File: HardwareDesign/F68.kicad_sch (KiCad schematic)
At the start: 2 parts, among them J001 Conn_02x40_Odd_Even

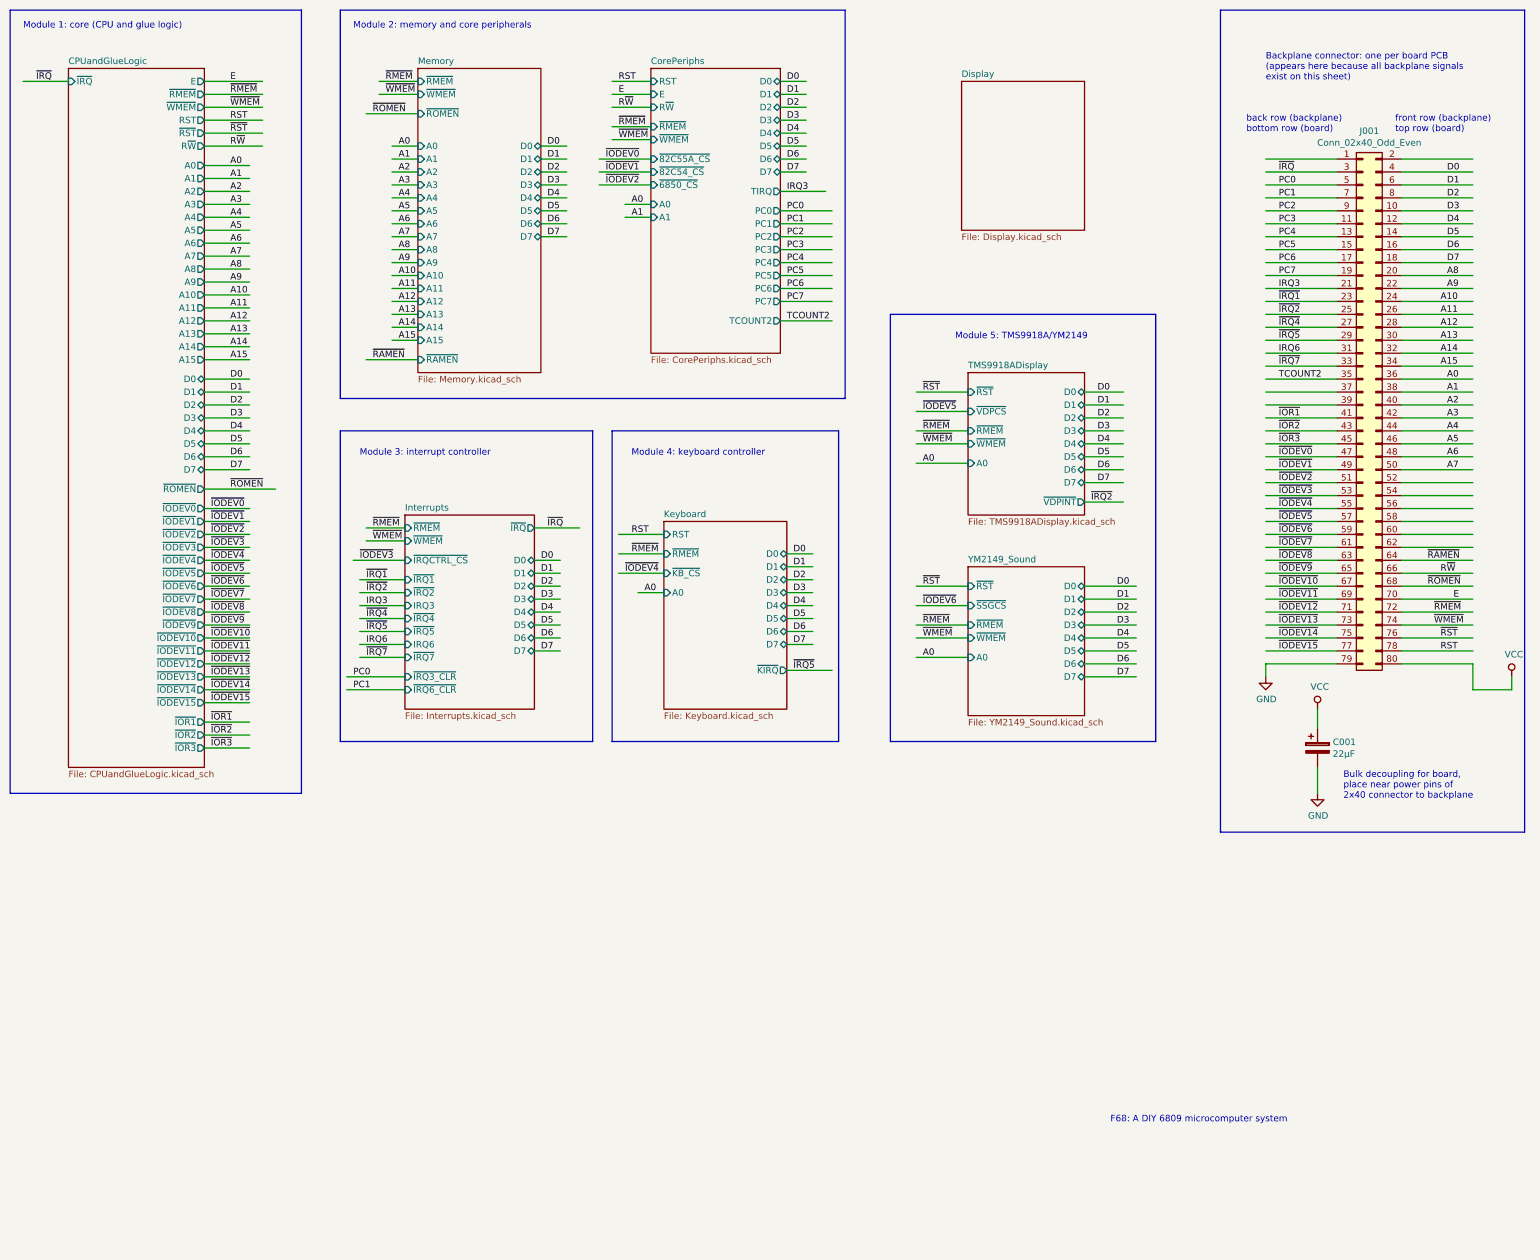
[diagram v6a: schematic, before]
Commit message: initial schematic for FPGA display controller
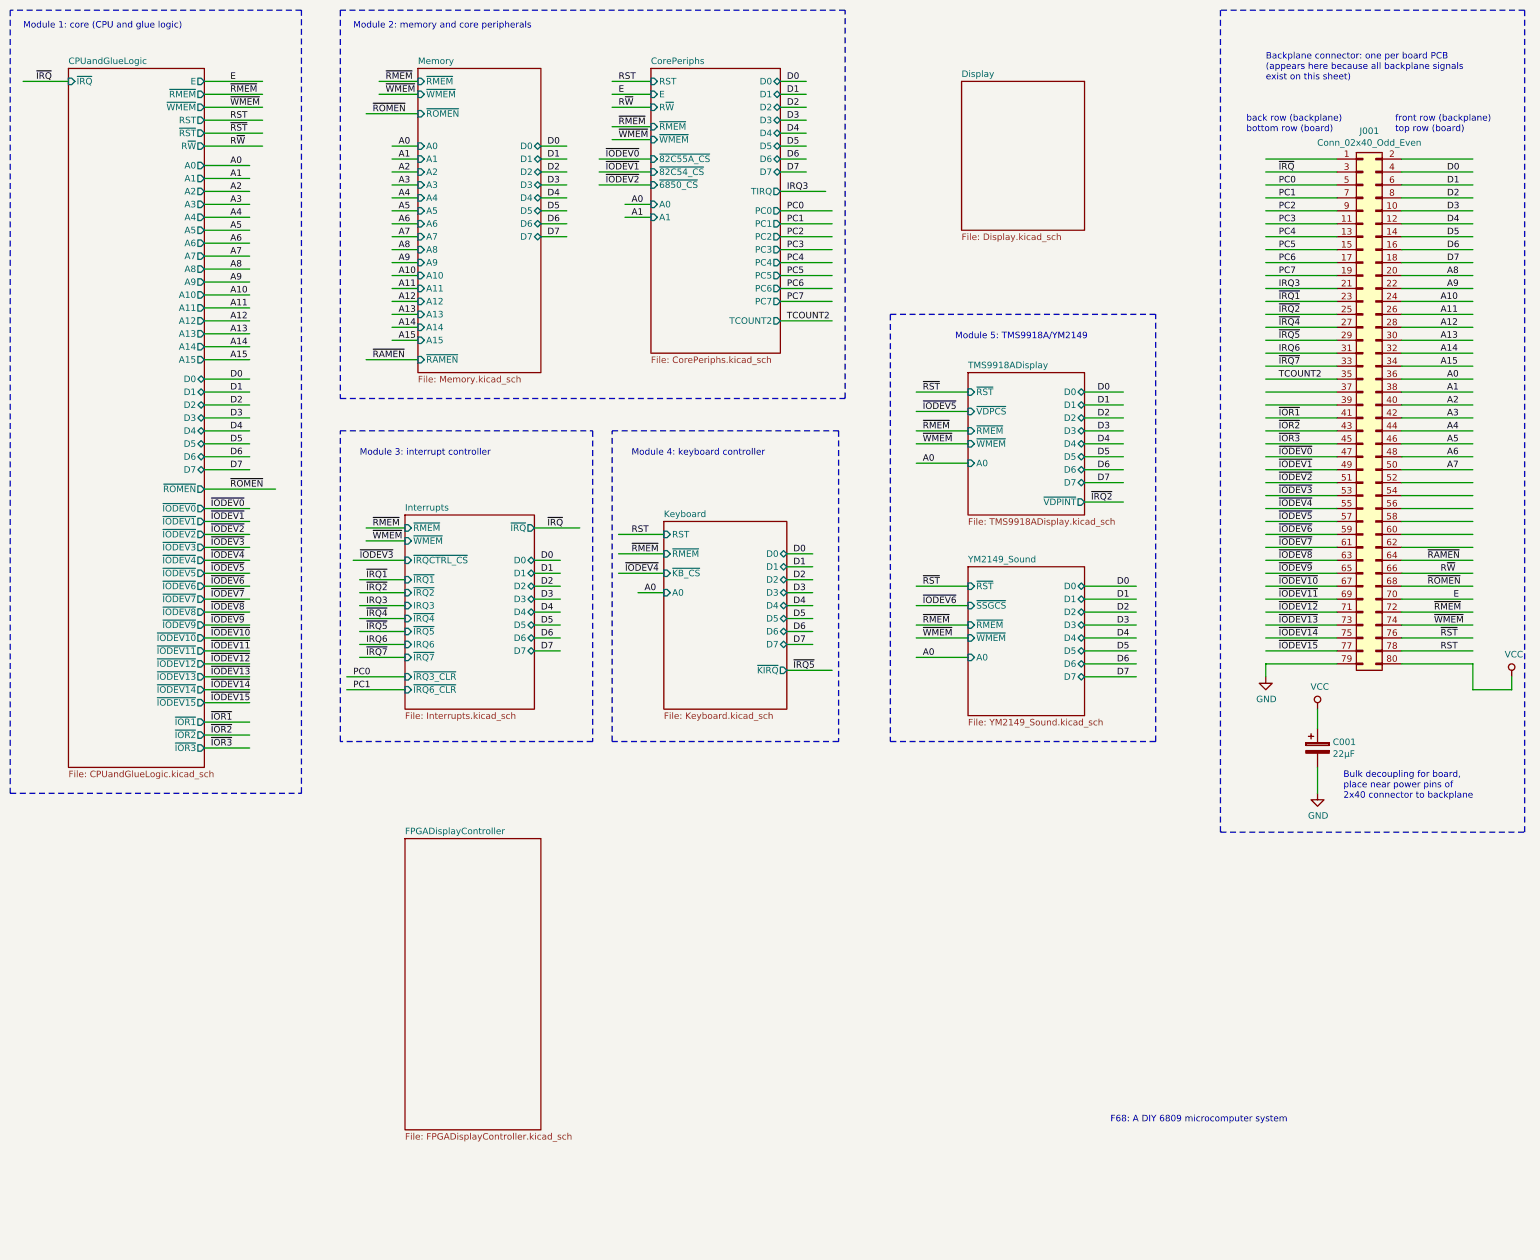
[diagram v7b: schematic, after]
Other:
- added sheet FPGADisplayController (FPGADisplayController.kicad_sch)

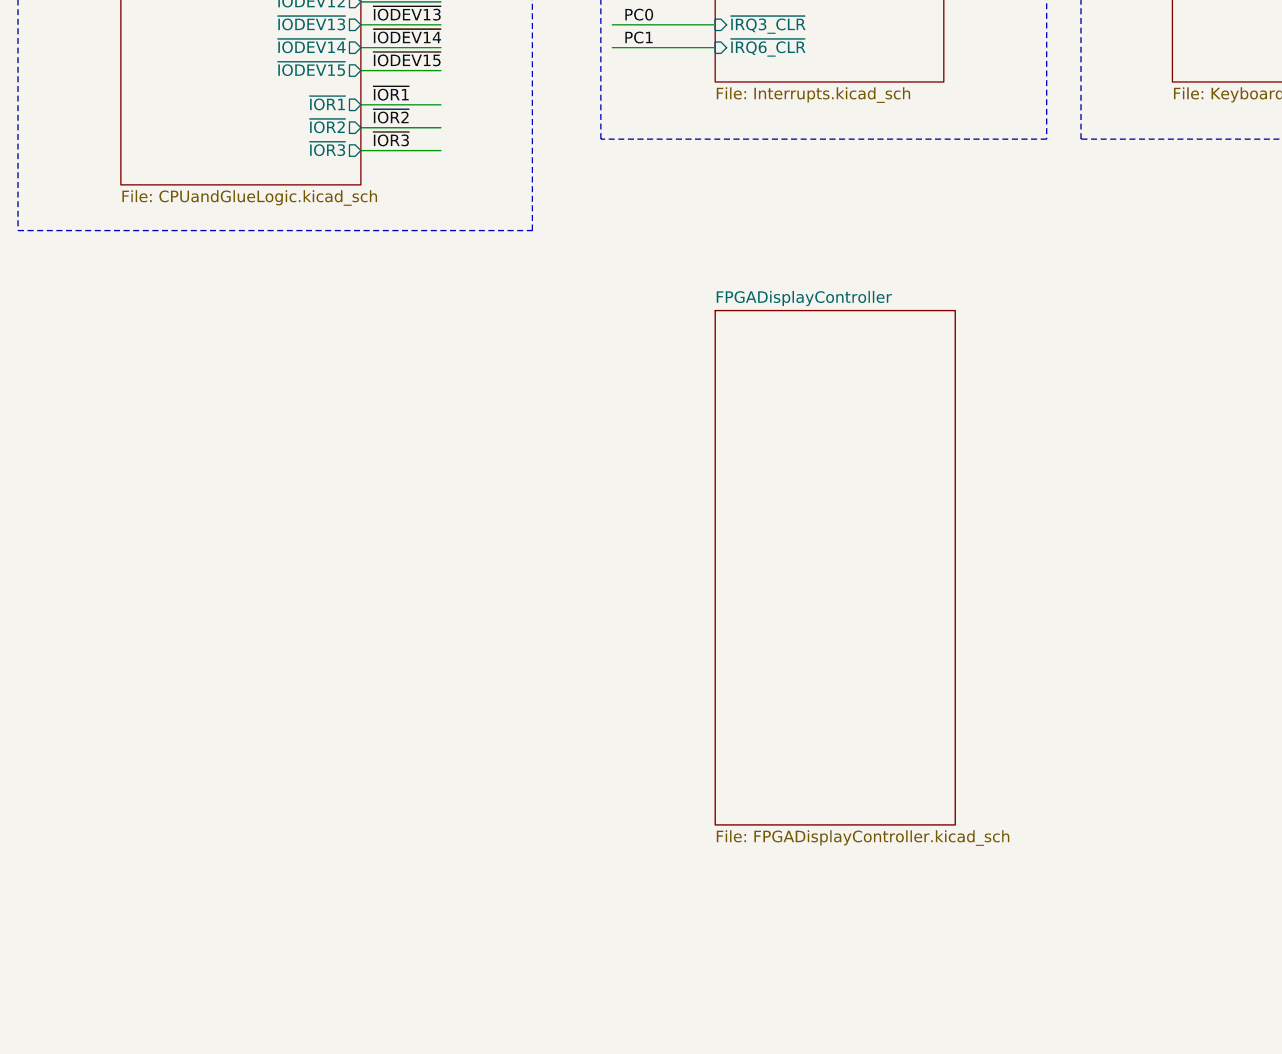
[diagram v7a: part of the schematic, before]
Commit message: connect signals to FPGA display controller module
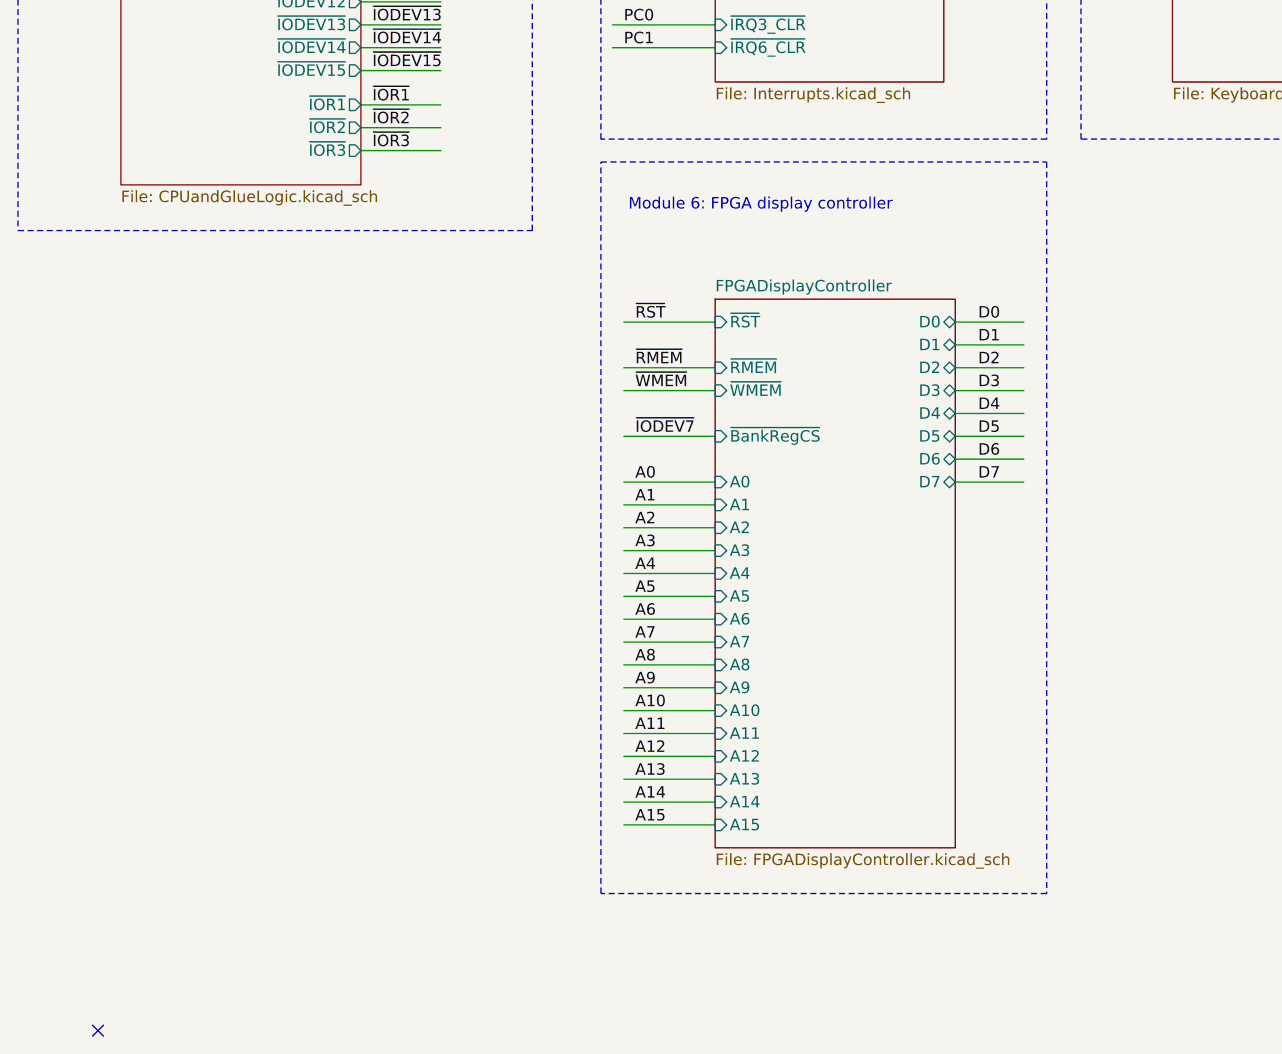
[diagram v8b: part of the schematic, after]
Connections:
- no-connect marks 0 -> 1
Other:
- sheet FPGADisplayController ports: added A0, A1, A10, A11, A12, A13, A14, A15, A2, A3, A4, A5, A6, A7, A8, A9, D0, D1, D2, D3, D4, D5, D6, D7, ~{BankRegCS}, ~{RMEM}, ~{RST}, ~{WMEM}; removed none
- note added: "Module 6: FPGA display controller"
